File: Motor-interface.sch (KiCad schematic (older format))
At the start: 40 parts, among them J101 0, J102 0, P101 TE-23pins connector, P102 PSU_ISO, P103 Halls, P104 LineContactor, P105 ReverseContactor, P106 FanContactor, P107 Battery+, P108 MC_USB, P109 MC_CAN, P110 HallCurrent, Q101 Q_NPN_BCE, U101 AP1117D50, U102 AP1117D33, U103 TLP2361, U104 TLP2361, U105 TLP2361, U106 TLP2361, U107 TLP2361, U108 TLP2361, U109 Teensy_3.2, U110 TLP2361, U111 FODM3052

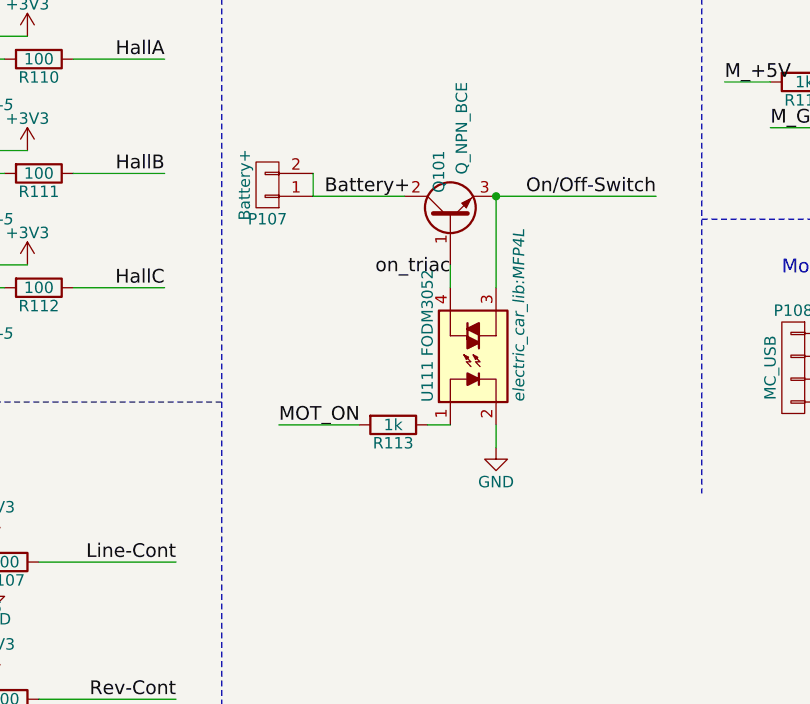
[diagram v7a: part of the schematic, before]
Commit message: fixed triac, passed DRC
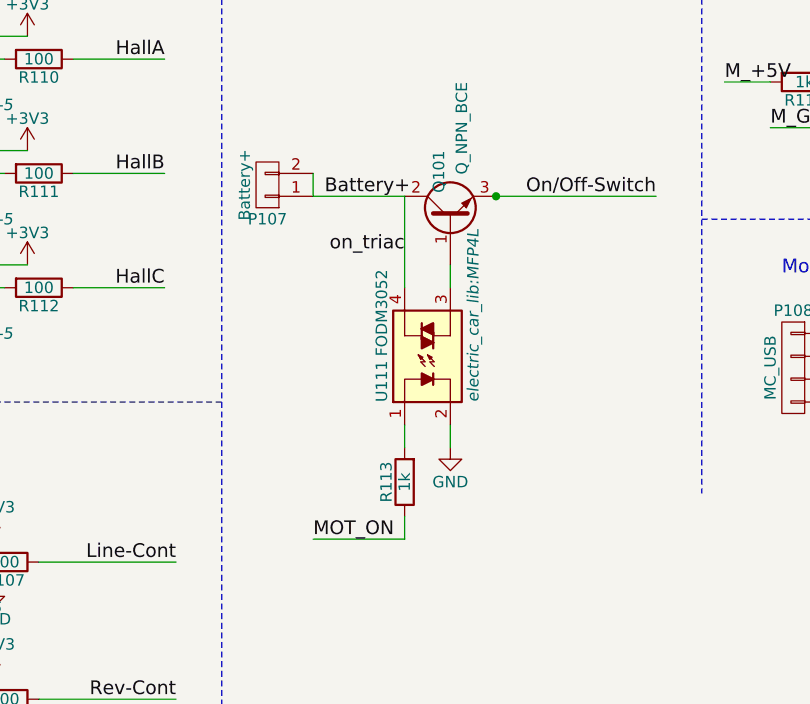
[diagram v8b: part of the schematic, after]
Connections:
- net Battery+: now also U111.4
- net MOT_ON: now also R113.1; no longer R113.2
- net On/Off-Switch: no longer U111.3
- net at U111.1: now also R113.2; no longer R113.1
- net on_triac: no longer names the net of Q101.1 (B)
- net on_triac: now also U111.3; no longer U111.4
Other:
- moved on the sheet: R113, U111
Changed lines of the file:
@@
 L GND #PWR01
 U 1 1 57FCC1C9
-P 7900 5500
-F 0 "#PWR01" H 7900 5250 50  0001 C CNN
-F 1 "GND" H 7900 5350 50  0000 C CNN
-F 2 "" H 7900 5500 50  0000 C CNN
-F 3 "" H 7900 5500 50  0000 C CNN
-	1    7900 5500
-	1    0    0    -1
-$EndComp
-Text Label 6950 5400 0    60   ~ 0
+P 7700 5500
+F 0 "#PWR01" H 7700 5250 50  0001 C CNN
+F 1 "GND" H 7700 5350 50  0000 C CNN
+F 2 "" H 7700 5500 50  0000 C CNN
+F 3 "" H 7700 5500 50  0000 C CNN
+	1    7700 5500
+	1    0    0    -1
+$EndComp
+Text Label 7100 5900 0    60   ~ 0
 MOT_ON
 Text Label 6200 1700 0    60   ~ 0
@@
 L R R113
 U 1 1 581878E6
-P 7450 5400
-F 0 "R113" V 7530 5400 50  0000 C CNN
-F 1 "1k" V 7450 5400 50  0000 C CNN
-F 2 "Resistors_SMD:R_1206_HandSoldering" V 7380 5400 50  0001 C CNN
-F 3 "" H 7450 5400 50  0000 C CNN
-	1    7450 5400
-	0    1    1    0
+P 7500 5650
+F 0 "R113" V 7580 5650 50  0000 C CNN
+F 1 "1k" V 7500 5650 50  0000 C CNN
+F 2 "Resistors_SMD:R_1206_HandSoldering" V 7430 5650 50  0001 C CNN
+F 3 "" H 7500 5650 50  0000 C CNN
+	1    7500 5650
+	-1   0    0    1
 $EndComp
 $Comp
@@
 Wire Wire Line
 	3200 6600 4300 6600
-Wire Wire Line
-	7600 5400 7700 5400
-Wire Wire Line
-	7300 5400 6950 5400
 Wire Notes Line
 	2600 600  2600 7150
@@
 L FODM3052 U111
 U 1 1 582C070F
-P 7800 5100
-F 0 "U111" H 7600 5300 50  0000 L CNN
-F 1 "FODM3052" H 7800 5300 50  0000 L CNN
-F 2 "electric_car_lib:MFP4L" H 7600 4900 50  0000 L CIN
-F 3 "" H 7775 5100 50  0000 L CNN
-	1    7800 5100
+P 7600 5100
+F 0 "U111" H 7400 5300 50  0000 L CNN
+F 1 "FODM3052" H 7600 5300 50  0000 L CNN
+F 2 "electric_car_lib:MFP4L" H 7400 4900 50  0000 L CIN
+F 3 "" H 7575 5100 50  0000 L CNN
+	1    7600 5100
 	0    -1   -1   0
 $EndComp
-Wire Wire Line
-	7700 4800 7700 4700
-Wire Wire Line
-	7900 4400 7900 4800
 Connection ~ 7900 4400
 Wire Wire Line
-	7900 5500 7900 5400
+	7700 5500 7700 5400
+Wire Wire Line
+	7100 4400 7500 4400
+$Comp
+L CONN_01X02 P107
+U 1 1 582C2C61
+P 6900 4350
+F 0 "P107" H 6900 4500 50  0000 C CNN
+F 1 "Battery+" V 7000 4350 50  0000 C CNN
+F 2 "Connect:bornier2" H 6900 4350 50  0001 C CNN
+F 3 "" H 6900 4350 50  0000 C CNN
+	1    6900 4350
+	-1   0    0    1
+$EndComp
+Wire Wire Line
+	7100 4300 7100 4400
+Text Label 3900 4800 2    59   ~ 0
+Motor-sensor-A
+Text Label 3900 5000 2    59   ~ 0
+Motor-sensor-B
+Text Label 3950 5200 2    59   ~ 0
+Motor-sensor-C
+Wire Wire Line
+	3700 4700 3100 4700
+Wire Wire Line
+	3100 4800 3900 4800
+Wire Wire Line
+	3700 4900 3100 4900
+Wire Wire Line
+	3100 5000 3900 5000
+Wire Wire Line
+	4050 5100 3100 5100
+Wire Wire Line
+	3100 5200 3950 5200
+Text Label 7150 4400 0    60   ~ 0
+Battery+
+Text Label 7500 4650 2    60   ~ 0
+on_triac
+$Comp
+L CONN_01X04 P110
+U 1 1 582D9085
+P 6000 1450
+F 0 "P110" H 6000 1700 50  0000 C CNN
+F 1 "HallCurrent" V 6100 1450 50  0000 C CNN
+F 2 "Pin_Headers:Pin_Header_Straight_1x04" H 6000 1450 50  0001 C CNN
+F 3 "" H 6000 1450 50  0000 C CNN
+	1    6000 1450
+	-1   0    0    -1
+$EndComp
+$Comp
+L +3V3 #PWR031
+U 1 1 582D980D
+P 6300 1300
+F 0 "#PWR031" H 6300 1150 50  0001 C CNN
+F 1 "+3V3" H 6300 1440 50  0000 C CNN
+F 2 "" H 6300 1300 50  0000 C CNN
+F 3 "" H 6300 1300 50  0000 C CNN
+	1    6300 1300
+	1    0    0    -1
+$EndComp
+$Comp
+L GND #PWR032
+U 1 1 582D98FC
+P 6550 1250
+F 0 "#PWR032" H 6550 1000 50  0001 C CNN
+F 1 "GND" H 6550 1100 50  0000 C CNN
+F 2 "" H 6550 1250 50  0000 C CNN
+F 3 "" H 6550 1250 50  0000 C CNN
+	1    6550 1250
+	1    0    0    -1
+$EndComp
+Wire Wire Line
+	6300 1300 6200 1300
+Wire Wire Line
+	6200 1400 6400 1400
+Wire Wire Line
+	6400 1400 6400 1250
+Wire Wire Line
+	6400 1250 6550 1250
+Wire Wire Line
+	6200 1500 7300 1500
+Wire Wire Line
+	6200 1600 7300 1600
+Text Label 6250 1500 0    60   ~ 0
+I_HallRef
+Text Label 6250 1600 0    60   ~ 0
+I_Hall
+Wire Wire Line
+	7300 2400 6200 2400
 $Comp
 L Q_NPN_BCE Q101
@@
 $EndComp
 Wire Wire Line
-	7100 4400 7500 4400
-$Comp
-L CONN_01X02 P107
-U 1 1 582C2C61
-P 6900 4350
-F 0 "P107" H 6900 4500 50  0000 C CNN
-F 1 "Battery+" V 7000 4350 50  0000 C CNN
-F 2 "Connect:bornier2" H 6900 4350 50  0001 C CNN
-F 3 "" H 6900 4350 50  0000 C CNN
-	1    6900 4350
-	-1   0    0    1
-$EndComp
-Wire Wire Line
-	7100 4300 7100 4400
-Text Label 3900 4800 2    59   ~ 0
-Motor-sensor-A
-Text Label 3900 5000 2    59   ~ 0
-Motor-sensor-B
-Text Label 3950 5200 2    59   ~ 0
-Motor-sensor-C
-Wire Wire Line
-	3700 4700 3100 4700
-Wire Wire Line
-	3100 4800 3900 4800
-Wire Wire Line
-	3700 4900 3100 4900
-Wire Wire Line
-	3100 5000 3900 5000
-Wire Wire Line
-	4050 5100 3100 5100
-Wire Wire Line
-	3100 5200 3950 5200
-Text Label 7150 4400 0    60   ~ 0
-Battery+
-Text Label 7700 4750 2    60   ~ 0
-on_triac
-$Comp
-L CONN_01X04 P110
-U 1 1 582D9085
-P 6000 1450
-F 0 "P110" H 6000 1700 50  0000 C CNN
-F 1 "HallCurrent" V 6100 1450 50  0000 C CNN
-F 2 "Pin_Headers:Pin_Header_Straight_1x04" H 6000 1450 50  0001 C CNN
-F 3 "" H 6000 1450 50  0000 C CNN
-	1    6000 1450
-	-1   0    0    -1
-$EndComp
-$Comp
-L +3V3 #PWR031
-U 1 1 582D980D
-P 6300 1300
-F 0 "#PWR031" H 6300 1150 50  0001 C CNN
-F 1 "+3V3" H 6300 1440 50  0000 C CNN
-F 2 "" H 6300 1300 50  0000 C CNN
-F 3 "" H 6300 1300 50  0000 C CNN
-	1    6300 1300
-	1    0    0    -1
-$EndComp
-$Comp
-L GND #PWR032
-U 1 1 582D98FC
-P 6550 1250
-F 0 "#PWR032" H 6550 1000 50  0001 C CNN
-F 1 "GND" H 6550 1100 50  0000 C CNN
-F 2 "" H 6550 1250 50  0000 C CNN
-F 3 "" H 6550 1250 50  0000 C CNN
-	1    6550 1250
-	1    0    0    -1
-$EndComp
-Wire Wire Line
-	6300 1300 6200 1300
-Wire Wire Line
-	6200 1400 6400 1400
-Wire Wire Line
-	6400 1400 6400 1250
-Wire Wire Line
-	6400 1250 6550 1250
-Wire Wire Line
-	6200 1500 7300 1500
-Wire Wire Line
-	6200 1600 7300 1600
-Text Label 6250 1500 0    60   ~ 0
-I_HallRef
-Text Label 6250 1600 0    60   ~ 0
-I_Hall
-Wire Wire Line
-	7300 2400 6200 2400
+	7500 5400 7500 5500
+Wire Wire Line
+	7100 5900 7500 5900
+Wire Wire Line
+	7500 5900 7500 5800
+Wire Wire Line
+	7700 4800 7700 4700
+Wire Wire Line
+	7500 4400 7500 4800
 $EndSCHEMATC
